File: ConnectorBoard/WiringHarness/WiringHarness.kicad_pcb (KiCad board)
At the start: 2 copper layers, 55 x 40 mm, 30 parts, among them J1 Barrel_Jack, J2 Conn_01x03, J3 Conn_01x03, J4 Conn_02x05_Odd_Even, J5 Socket, J6 Qwiic, J7 Header, U2 TLV75533PDBV, U3 NCP1117-ADJ_SOT223

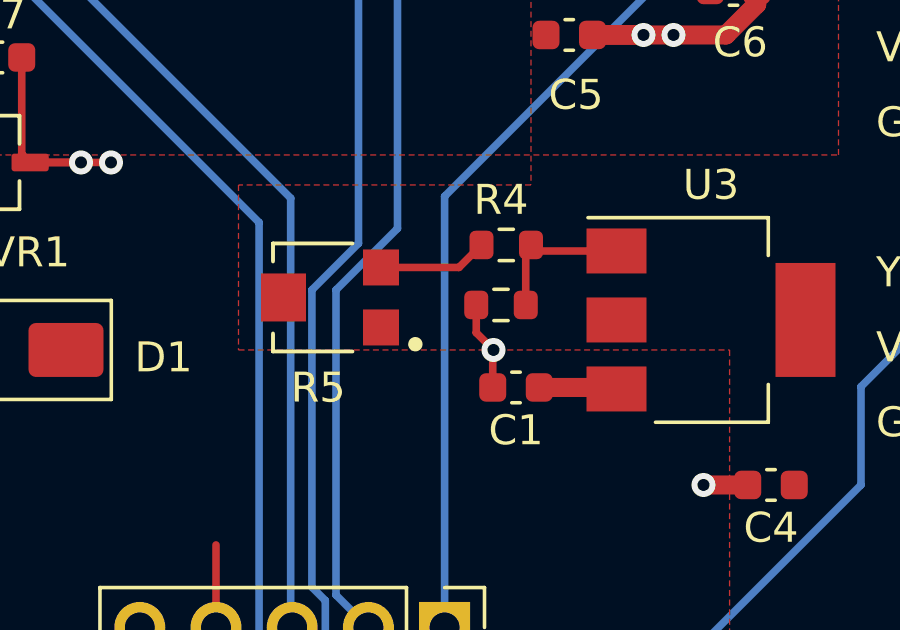
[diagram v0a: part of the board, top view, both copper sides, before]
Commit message: Fix the bias network on the regulator.
Close #6
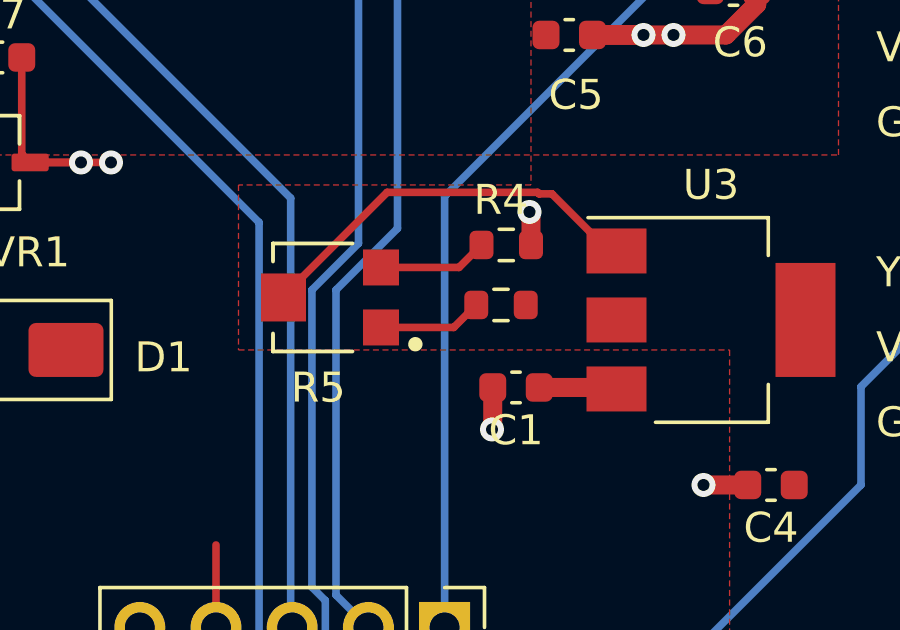
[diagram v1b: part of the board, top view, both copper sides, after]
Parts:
- R3: value 100 -> 1K
- R4: value 300 -> 330
- R5: value 200 -> TC33X-2-201E
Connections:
- R3 pad 1: Net-(U3-ADJ) -> /VoutServo
- R3 pad 2: GND -> Net-(R3-Pad2)
- R4 pad 1: Net-(U3-ADJ) -> GND
- R5 pad 1: unconnected-(R5-Pad1) -> Net-(R3-Pad2)
- R5 pad 2: /VoutServo -> Net-(U3-ADJ)
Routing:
- net Net-(U3-ADJ): track 5.01 -> 13.4 mm
- net Net-(R3-Pad2): track 0.00 -> 3.49 mm
- net GND: track 29.4 -> 29.0 mm, vias 11 -> 12

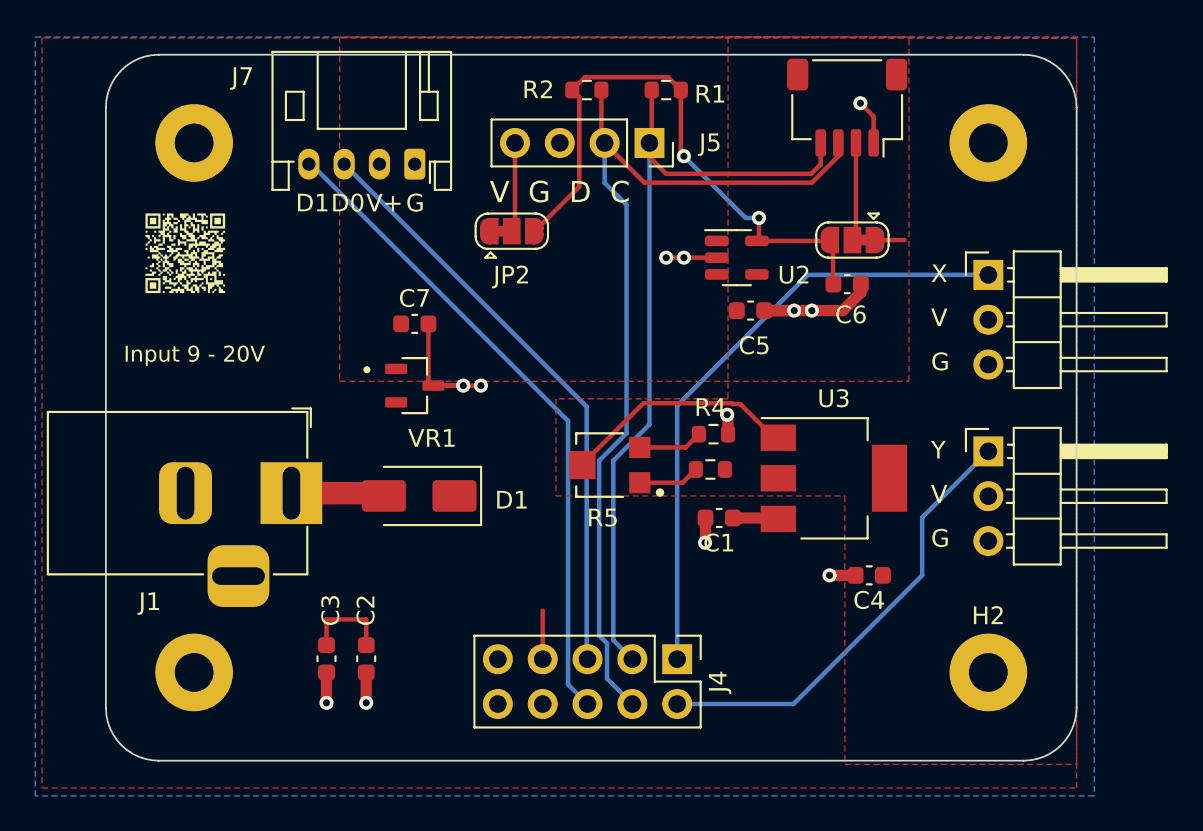
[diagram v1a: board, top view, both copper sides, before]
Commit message: Work on #10.
Need to decide if the leadless package is easier to deal with than a small BGA.

Not obvious it is.
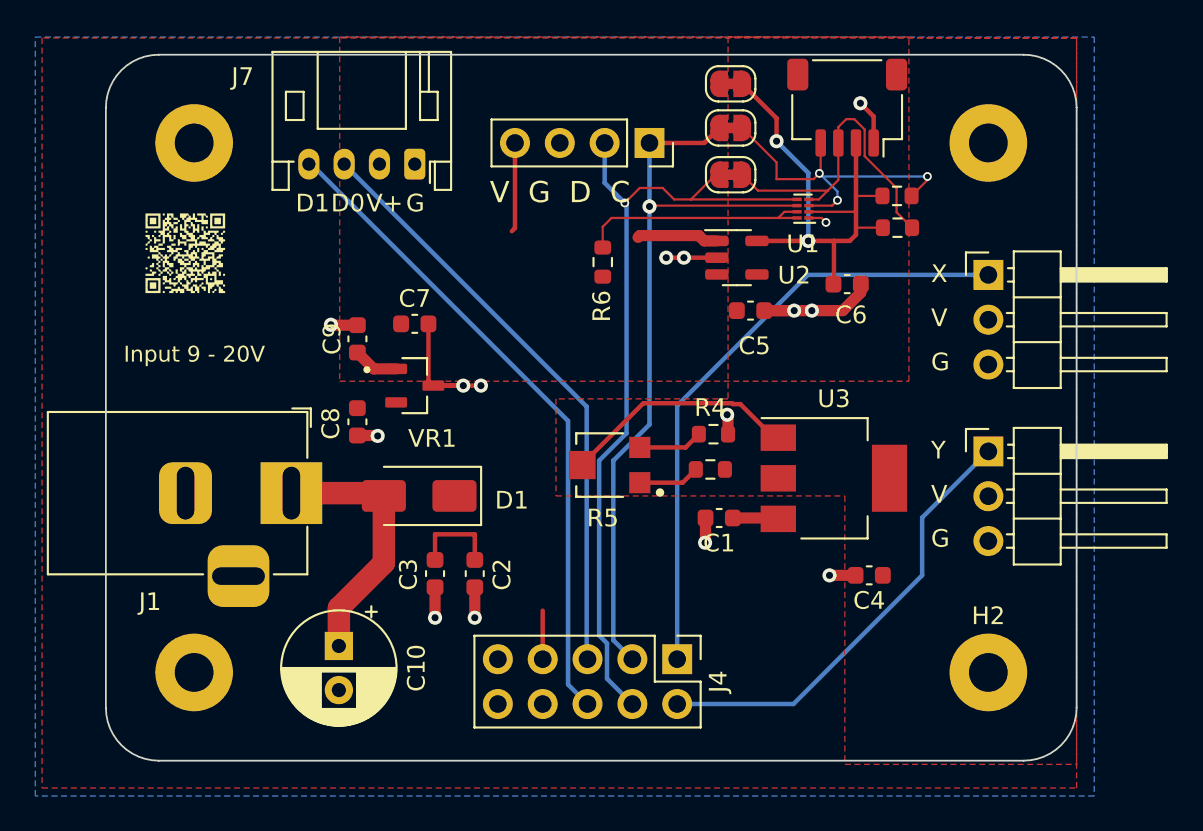
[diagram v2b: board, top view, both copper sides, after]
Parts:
- added C10: 22uF, Capacitor_THT:CP_Radial_D6.3mm_P2.50mm, F.Cu at (140.2, 109.2)
- added C8: 0.1uF, Capacitor_SMD:C_0603_1608Metric, F.Cu at (141.2, 96.5)
- added C9: 0.1uF, Capacitor_SMD:C_0603_1608Metric, F.Cu at (141.2, 91.8)
- added JP3: SolderJumper_2_Bridged, Jumper:SolderJumper-2_P1.3mm_Bridged_RoundedPad1.0x1.5mm, F.Cu at (162.4, 77.4)
- added R6: 200k, Resistor_SMD:R_0603_1608Metric, F.Cu at (155.2, 87.5)
- added U1: PCA9306DQER, Package_SON:X2SON-8_1.4x1mm_P0.35mm, F.Cu at (166.5, 84.5)
- JP1, JP2: value SolderJumper_3_Bridged12 -> SolderJumper_2_Bridged; footprint Jumper:SolderJumper-3_P1.3mm_Bridged12_RoundedPad1.0x1.5mm -> Jumper:SolderJumper-2_P1.3mm_Bridged_RoundedPad1.0x1.5mm
- moved R2 19.3 mm to (171.8, 85.5)
- moved R1 14.4 mm to (171.8, 83.8), turned to 0 degrees
- moved JP2 12.8 mm to (162.4, 82.5)
- moved JP1 9.38 mm to (162.4, 79.9), turned to 0 degrees
- moved C2 7.82 mm to (147.9, 105.2)
- moved C3 7.82 mm to (145.7, 105.2)
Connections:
- J5 pad 4: Net-(J5-Pin_4) -> /IIC5V
- J6 pad 2: Net-(J6-Pin_2) -> /IIC3V
- J6 pad 3: /SDA -> /SDA3
- J6 pad 4: /SCL -> /SCL3
- JP1 pad 1: /IIC5V -> /SCL
- JP1 pad 2: Net-(J6-Pin_2) -> /SCL3
- JP2 pad 1: /IIC5V -> /SDA
- JP2 pad 2: Net-(J5-Pin_4) -> /SDA3
- R1 pad 2: /SCL -> /SCL3
- R2 pad 2: /SDA -> /SDA3
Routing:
- net /SCL3: track 0.00 -> 19.2 mm, vias 0 -> 3
- net /SDA3: track 0.00 -> 18.8 mm
- net Net-(U1-EN): track 0.00 -> 13.3 mm
- net /IIC5V: track 1.45 -> 12.3 mm
- net Net-(D1-A): track 5.57 -> 15.1 mm
- net /SDA: track 52.3 -> 46.1 mm, vias 0 -> 1
- net Net-(J6-Pin_2): track 5.50 -> 0.00 mm
- net Net-(J5-Pin_4): track 5.07 -> 0.00 mm
- net /IIC3V: track 33.7 -> 29.4 mm
- net GND: track 29.0 -> 32.6 mm, vias 12 -> 15
- net /SCL: track 45.9 -> 43.0 mm, vias 0 -> 1

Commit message: signal caps at servo connectors
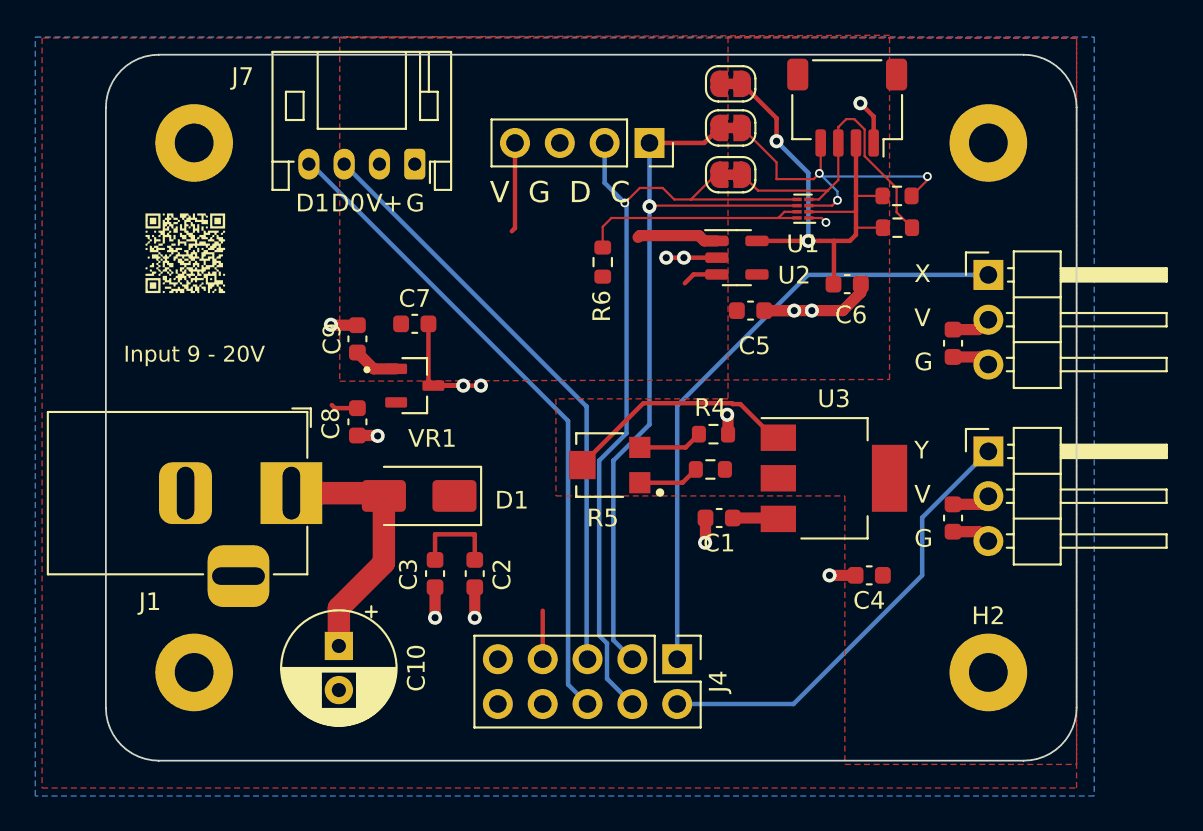
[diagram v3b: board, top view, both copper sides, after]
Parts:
- added C11: 0.1uF, Capacitor_SMD:C_0603_1608Metric, F.Cu at (175.0, 92.1)
- added C12: 0.1uF, Capacitor_SMD:C_0603_1608Metric, F.Cu at (175.0, 102.0)
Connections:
- J4 pad 10: unconnected-(J4-Pin_10-Pad10) -> GND
- J4 pad 8: unconnected-(J4-Pin_8-Pad8) -> /Vsys
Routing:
- net /VoutServo: track 0.00 -> 4.42 mm
- net GND: track 32.6 -> 37.0 mm
- net /IIC5V: track 12.3 -> 14.3 mm
- net /Vsys: track 10.5 -> 12.0 mm

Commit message: Add QR code in preparation for next release
Add Cap to

5V

Buttons

Add level shifter.

Close #7
Close #9
Close #11
Close #14
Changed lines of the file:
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@@
     (effects (font (size 1 1) (thickness 0.15)) (justify left bottom))
   )
-  (gr_text "Input 9 - 20V" (at 128 93.25) (layer "F.SilkS")
+  (gr_text "Input 9 - 20V" (at 128 94.75) (layer "F.SilkS")
     (effects (font (size 0.9 0.9) (thickness 0.09)) (justify left bottom))
   )

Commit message: Change footprint for level shifter to something more reasonable.
Add lots of cap to controller.

Add level shifter to controller
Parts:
- U1: footprint Package_SON:X2SON-8_1.4x1mm_P0.35mm -> Package_SO:TSSOP-8_3x3mm_P0.65mm
- moved R2 2.60 mm to (173.7, 83.7), turned to 180 degrees
- moved R1 2.45 mm to (173.7, 85.3), turned to 180 degrees
- moved U1 2.12 mm to (168.6, 84.7)
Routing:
- net /IIC3V: track 29.4 -> 34.8 mm
- net /SCL3: track 19.2 -> 24.1 mm, vias 3 -> 2
- net /SDA3: track 18.8 -> 20.8 mm
- net Net-(U1-EN): track 13.3 -> 12.6 mm
- net /SDA: track 46.1 -> 45.5 mm
- net /SCL: track 43.0 -> 43.5 mm

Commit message: update qr code and legend
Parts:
- removed the G*** at (131.5, 87.0)
- added G***: LOGO, QRCodeLibrary:v0.9, B.Cu at (168.1, 105.9)
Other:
- board text added: "ENGS28 Maze Controller wiring harness V0.9 - Tad Truex Copyright 2023, Dartmouth College"
- board text removed: "ENGS28 Maze Controller wiring harness V0.5wh - Tad Truex Copyright 2023, Dartmouth College"

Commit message: Hard to believe, but I had the resistors backward again on the regulator...
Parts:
- R3: value 1K -> 300
- R4: value 330 -> 1K
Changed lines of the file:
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@@
     (descr "Resistor SMD 0603 (1608 Metric), square (rectangular) end terminal, IPC_7351 nominal, (Body size source: IPC-SM-782 page 72, https://www.pcb-3d.com/wordpress/wp-content/uploads/ipc-sm-782a_amendment_1_and_2.pdf), generated with kicad-footprint-generator")
     (tags "resistor")
-    (property "Digikey" "RMCF0603FT300RCT-ND")
+    (property "Digikey" "")
     (property "Sheetfile" "WiringHarness.kicad_sch")
     (property "Sheetname" "")
-    (property "Vendor" "RMCF0603FT300RCT-ND")
+    (property "Vendor" "")
     (property "ki_description" "Resistor, small US symbol")
     (property "ki_keywords" "r resistor")
@@
         (effects (font (size 1 1) (thickness 0.15)))
     )
-    (fp_text value "330" (at 0 1.43) (layer "F.Fab")
+    (fp_text value "1K" (at 0 1.43) (layer "F.Fab")
         (effects (font (size 1 1) (thickness 0.15)))
     )
@@
     (descr "Resistor SMD 0603 (1608 Metric), square (rectangular) end terminal, IPC_7351 nominal, (Body size source: IPC-SM-782 page 72, https://www.pcb-3d.com/wordpress/wp-content/uploads/ipc-sm-782a_amendment_1_and_2.pdf), generated with kicad-footprint-generator")
     (tags "resistor")
-    (property "Digikey" "RMCF0603FT100RCT-ND")
+    (property "Digikey" "RMCF0603FT300RCT-ND")
     (property "Sheetfile" "WiringHarness.kicad_sch")
     (property "Sheetname" "")
-    (property "Vendor" "RMCF0603FT100RCT-ND")
+    (property "Vendor" "RMCF0603FT300RCT-ND")
     (property "ki_description" "Resistor, small US symbol")
     (property "ki_keywords" "r resistor")
@@
         (effects (font (size 1 1) (thickness 0.15)))
     )
-    (fp_text value "1K" (at 0 1.43) (layer "F.Fab")
+    (fp_text value "300" (at 0 1.43) (layer "F.Fab")
         (effects (font (size 1 1) (thickness 0.15)))
     )
